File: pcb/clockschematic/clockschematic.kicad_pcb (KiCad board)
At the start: 2 copper layers, 121.9 x 96.5 mm, 19 parts, among them SW1 SW_Push, SW2 SW_Push, SW3 SW_Push, SW4 SW_Push, U0 RPi_Pico_TH, U1 RDA5807M_Module, U2 LM386, U3 LM386

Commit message: update
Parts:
- added J1: Barrel_Jack, Connector_BarrelJack:BarrelJack_CUI_PJ-063AH_Horizontal, B.Cu at (190.5, 102.1)
- moved U2 5.08 mm to (106.7, 55.9)
- moved C1 5.08 mm to (109.2, 66.0)
- moved C2 5.08 mm to (109.2, 73.7)
- moved LS1 5.08 mm to (101.6, 94.0)
- moved R3 5.08 mm to (101.6, 73.7)
- moved R1 1.90 mm to (200.4, 82.5)
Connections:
- U0 pad 40: unconnected-(U0-Pad40) -> +5V
- U2 pad 6: +3.3V -> +5V
- U3 pad 6: +3.3V -> +5V
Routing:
- net +5V: track 0.00 -> 120.9 mm
- net (no net): track 0.00 -> 96.5 mm, vias 0 -> 168
- net +3.3V: track 138.3 -> 87.5 mm
- net Net-(SW4-Pad2): track 91.3 -> 97.8 mm
- net Net-(SW3-Pad2): track 66.4 -> 72.9 mm
- net Net-(SW2-Pad2): track 36.3 -> 42.8 mm
- net Net-(SW1-Pad2): track 12.4 -> 18.9 mm
- net Net-(U1-Pad8): track 41.6 -> 36.5 mm
- net Net-(R1-Pad2): track 80.0 -> 75.1 mm
- net Net-(R2-Pad2): track 73.3 -> 70.3 mm
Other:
- board size 121.9 x 96.5 mm -> 111.8 x 91.4 mm

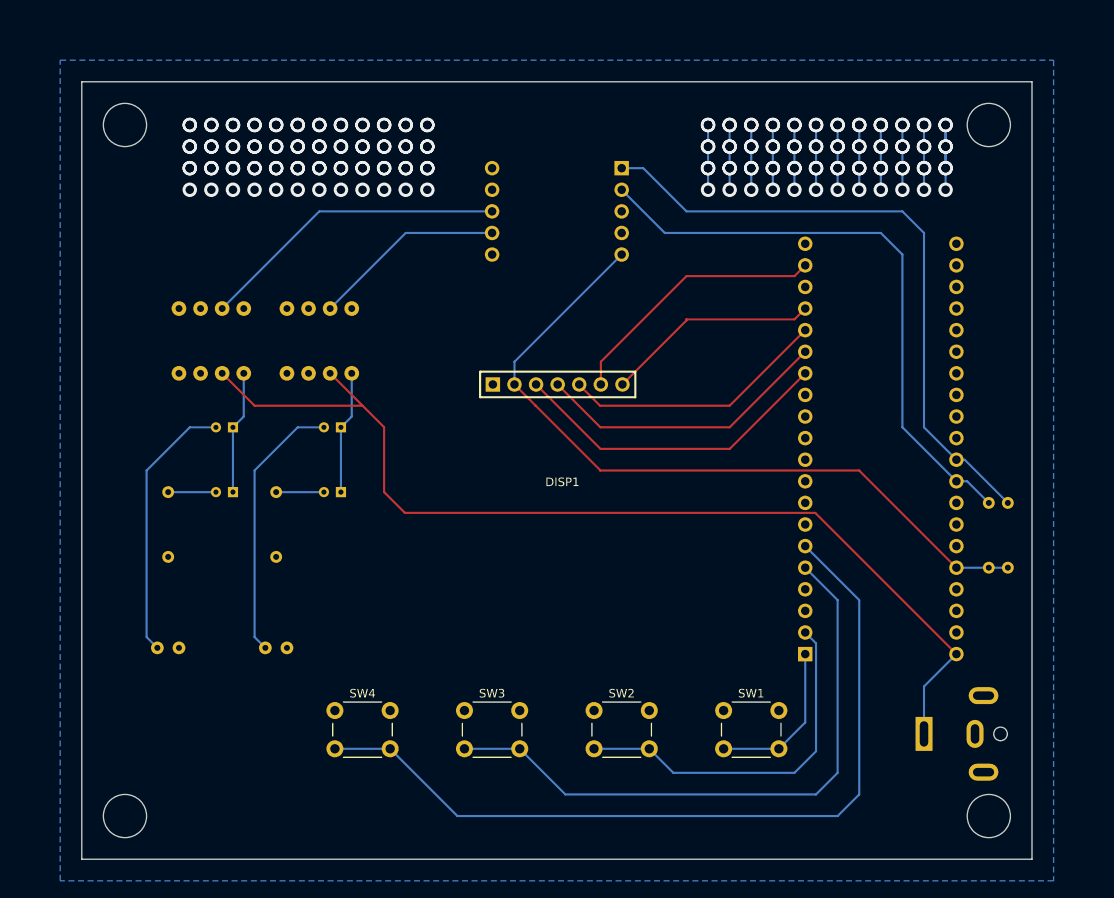
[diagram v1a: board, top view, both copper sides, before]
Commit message: time is working display is working radio is working new pcb
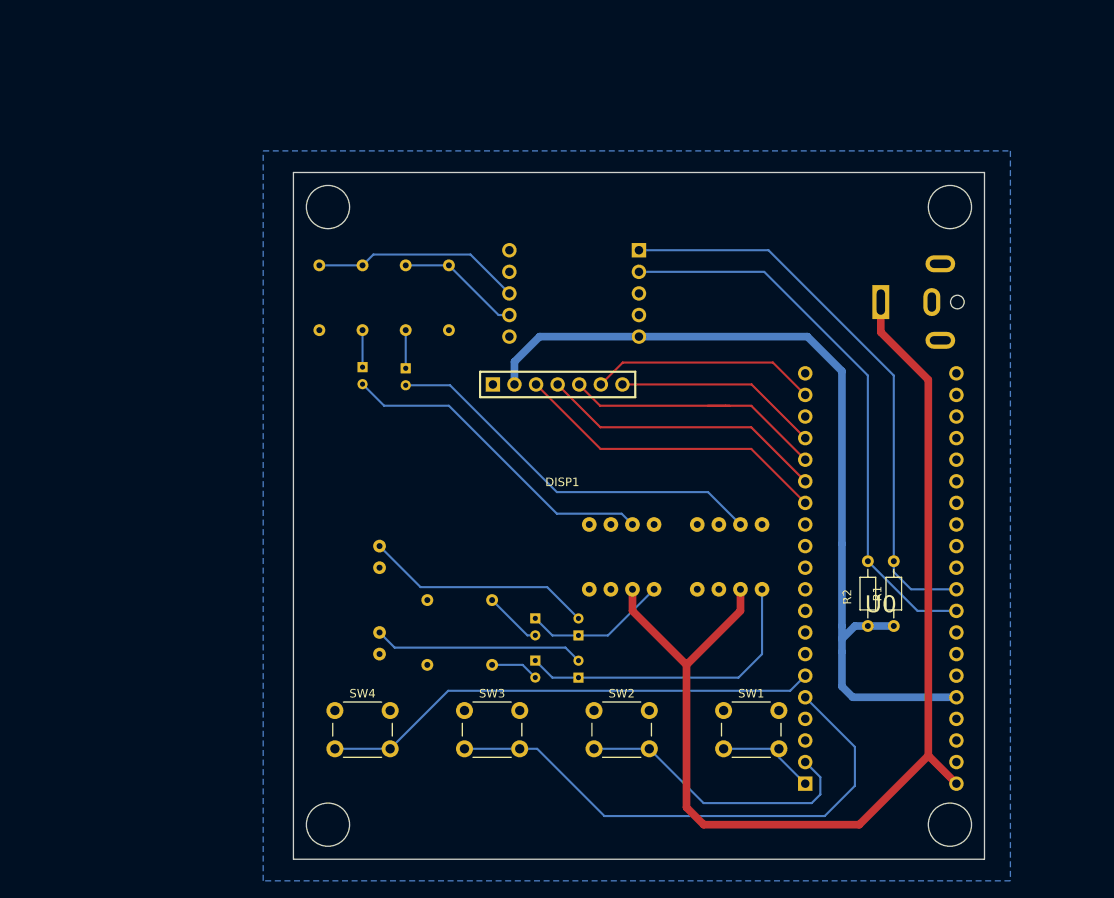
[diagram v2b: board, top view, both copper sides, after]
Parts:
- added C5: 10µF, Capacitor_THT:CP_Radial_D4.0mm_P2.00mm, B.Cu at (129.5, 59.1)
- added C6: 10µF, Capacitor_THT:CP_Radial_D4.0mm_P2.00mm, B.Cu at (124.5, 59.0)
- added R5: 10k, Resistor_THT:R_Axial_DIN0204_L3.6mm_D1.6mm_P7.62mm_Horizontal, B.Cu at (124.5, 47.0)
- added R6: 2k, Resistor_THT:R_Axial_DIN0204_L3.6mm_D1.6mm_P7.62mm_Horizontal, B.Cu at (119.4, 47.0)
- added R7: 10k, Resistor_THT:R_Axial_DIN0204_L3.6mm_D1.6mm_P7.62mm_Horizontal, B.Cu at (129.5, 47.0)
- added R8: 2k, Resistor_THT:R_Axial_DIN0204_L3.6mm_D1.6mm_P7.62mm_Horizontal, B.Cu at (134.6, 54.6)
- R1, R2: moved to F.Cu
- moved U2 54.5 mm to (154.9, 81.3)
- moved U3 54.5 mm to (167.6, 81.3)
- moved J1 51.0 mm to (185.4, 51.3)
- moved C1 47.4 mm to (149.9, 90.5), turned to 90 degrees
- moved C3 40.6 mm to (149.9, 95.5), turned to 90 degrees
- moved R3 40.2 mm to (139.7, 86.4), turned to 180 degrees
- moved C2 38.5 mm to (144.8, 88.5), turned to -90 degrees
- moved R4 32.5 mm to (139.7, 94.0), turned to 180 degrees
- moved C4 30.3 mm to (144.8, 93.5), turned to -90 degrees
- moved LS1 26.2 mm to (124.5, 81.3), turned to 90 degrees
- moved R2 15.8 mm to (183.9, 89.4)
- moved U0 15.2 mm to (185.4, 83.8)
- moved R1 15.1 mm to (186.9, 89.4)
- moved LS2 10.5 mm to (124.5, 91.4), turned to 90 degrees
- moved U1 9.86 mm to (149.4, 50.3)
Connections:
- net Net-(SW4-Pad2) renamed Internal PullUp R
- U2 pad 3: Net-(U1-Pad8) -> Net-(U2-Pad3)
- U3 pad 3: Net-(U1-Pad7) -> Net-(U3-Pad3)
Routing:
- net (no net): track 96.5 -> 0.00 mm, vias 168 -> 0
- net Net-(U3-Pad3): track 0.00 -> 46.2 mm
- net Internal PullUp R: track 97.8 -> 58.9 mm
- net Net-(U2-Pad3): track 0.00 -> 38.6 mm
- net Net-(C3-Pad1): track 14.5 -> 36.3 mm
- net +3.3V: track 87.5 -> 101.9 mm
- net +5V: track 120.9 -> 132.8 mm
- net Net-(U1-Pad8): track 36.5 -> 24.8 mm
- net Net-(SW3-Pad2): track 72.9 -> 63.5 mm
- net Net-(SW2-Pad2): track 42.8 -> 34.2 mm
- net Net-(U1-Pad7): track 22.7 -> 14.6 mm
- net Net-(R1-Pad2): track 75.1 -> 67.4 mm
- net Net-(SW1-Pad2): track 18.9 -> 11.9 mm
- net Net-(C3-Pad2): track 31.7 -> 24.8 mm
- net Net-(DISP1-Pad6): track 31.4 -> 26.7 mm
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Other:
- board size 111.8 x 91.4 mm -> 81.3 x 80.8 mm
